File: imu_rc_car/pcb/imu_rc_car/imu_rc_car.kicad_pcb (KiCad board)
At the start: 2 copper layers, 100.8 x 82.3 mm, 0 parts

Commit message: commit #26
started work car pcb
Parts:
- added C10: 10uF, Capacitor_SMD:C_1206_3216Metric_Pad1.33x1.80mm_HandSolder, F.Cu at (168.7, 98.1)
- added C11: 0.1uF, Capacitor_SMD:C_1206_3216Metric_Pad1.33x1.80mm_HandSolder, F.Cu at (167.1, 116.6)
- added C12: 10uF, Capacitor_SMD:C_1206_3216Metric_Pad1.33x1.80mm_HandSolder, F.Cu at (167.1, 121.1)
- added C13: 0.1uF, Capacitor_SMD:C_1206_3216Metric_Pad1.33x1.80mm_HandSolder, F.Cu at (180.9, 109.6)
- added C14: 10uF, Capacitor_SMD:C_1206_3216Metric_Pad1.33x1.80mm_HandSolder, F.Cu at (183.5, 109.6)
- added C15: 0.1uF, Capacitor_SMD:C_1206_3216Metric_Pad1.33x1.80mm_HandSolder, F.Cu at (178.3, 109.6)
- added C16: 10uF, Capacitor_SMD:C_1206_3216Metric_Pad1.33x1.80mm_HandSolder, F.Cu at (175.6, 109.6)
- added C7: 1uF/16V, Capacitor_SMD:C_0805_2012Metric, F.Cu at (164.4, 73.4)
- added C8: 1uF/16V, Capacitor_SMD:C_0805_2012Metric, F.Cu at (164.4, 76.9)
- added C9: 0.1uF, Capacitor_SMD:C_1206_3216Metric_Pad1.33x1.80mm_HandSolder, F.Cu at (168.7, 102.1)
- added J1: Encoder FS, Connector_JST:JST_PH_S4B-PH-K_1x04_P2.00mm_Horizontal, F.Cu at (146.0, 62.0)
- added J10: Prox Sensor RS, Connector_JST:JST_PH_S5B-PH-K_1x05_P2.00mm_Horizontal, F.Cu at (136.0, 128.6)
- added J11: Prox Sensor LS, Connector_JST:JST_PH_S5B-PH-K_1x05_P2.00mm_Horizontal, F.Cu at (121.0, 128.6)
- added J12: Prox Sensor BS, Connector_JST:JST_PH_S5B-PH-K_1x05_P2.00mm_Horizontal, F.Cu at (106.0, 128.6)
- added J2: Encoder BS, Connector_JST:JST_PH_S4B-PH-K_1x04_P2.00mm_Horizontal, F.Cu at (165.5, 62.0)
- added J7: Left Terminal, TerminalBlock:TerminalBlock_Xinya_XY308-2.54-4P_1x04_P2.54mm_Horizontal, F.Cu at (165.4, 131.5)
- added J8: Right Terminal, TerminalBlock:TerminalBlock_Xinya_XY308-2.54-4P_1x04_P2.54mm_Horizontal, F.Cu at (177.4, 131.5)
- added J9: Prox Sensor FS, Connector_JST:JST_PH_S5B-PH-K_1x05_P2.00mm_Horizontal, F.Cu at (151.0, 128.6)
- added Q5: IRLML6344TRPBF, Package_TO_SOT_SMD:SOT-23, F.Cu at (146.4, 74.8)
- added Q6: DMP3160L-7, Package_TO_SOT_SMD:SOT-23, F.Cu at (140.5, 74.9)
- added R10: 6k, Resistor_SMD:R_0805_2012Metric, F.Cu at (142.5, 79.9)
- added R8: 10k, Resistor_SMD:R_0805_2012Metric, F.Cu at (144.9, 70.9)
- added R9: 22k, Resistor_SMD:R_0805_2012Metric, F.Cu at (147.3, 79.9)
- added U1: ESP32-S3-DevKitC, PCM_Espressif:ESP32-S3-DevKitC, F.Cu at (127.9, 117.3)
- added U2: TB6612FNG, Package_SO:SSOP-24_5.3x8.2mm_P0.65mm, F.Cu at (168.7, 109.1)
- added U3: AP2112K-3.3, Package_TO_SOT_SMD:SOT-23-5, F.Cu at (159.9, 74.7)
- added U4: TB6612FNG, Package_SO:SSOP-24_5.3x8.2mm_P0.65mm, F.Cu at (181.9, 117.3)
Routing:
- net +3V3: track 0.00 -> 78.5 mm
- net Net-(Q5-D): track 0.00 -> 20.5 mm
- net +BATT: track 0.00 -> 13.6 mm
- net Net-(Q6-S): track 0.00 -> 4.13 mm
- net BATT_READ: track 0.00 -> 3.00 mm
- added copper zone on F.Cu, net GND
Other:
- board size 100.8 x 82.3 mm -> 100 x 82.3 mm

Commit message: commit #27
revision for hand unit complete (board is ready)
board for proximity sensors in series
minor revision in encoder board
progressing work in car board
added essential libraries support for 3D components
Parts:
- removed C7, C8: 1uF/16V, Capacitor_SMD:C_0805_2012Metric
- removed J10: Prox Sensor RS, Connector_JST:JST_PH_S5B-PH-K_1x05_P2.00mm_Horizontal
- removed J11: Prox Sensor LS, Connector_JST:JST_PH_S5B-PH-K_1x05_P2.00mm_Horizontal
- removed J12: Prox Sensor BS, Connector_JST:JST_PH_S5B-PH-K_1x05_P2.00mm_Horizontal
- removed Q5: IRLML6344TRPBF, Package_TO_SOT_SMD:SOT-23
- removed Q6: DMP3160L-7, Package_TO_SOT_SMD:SOT-23
- removed U4: TB6612FNG, Package_SO:SSOP-24_5.3x8.2mm_P0.65mm
- added C1: 10uF, Capacitor_SMD:CP_Elec_5x5.7, F.Cu at (184.1, 68.4)
- added J3: Encoder B, IMURCLibrary:JST_PH_S4B-PH-SM4-TB_1x04-1MP_P2.00mm_Horizontal, B.Cu at (145.0, 131.8)
- added J4: Prox Sensor FS, IMURCLibrary:JST_PH_S5B-PH-SM4-TB_1x05-1MP_P2.00mm_Horizontal, F.Cu at (127.3, 131.8)
- added J5: Prox Sensor LS, IMURCLibrary:JST_PH_S5B-PH-SM4-TB_1x05-1MP_P2.00mm_Horizontal, B.Cu at (127.3, 131.8)
- added J6: Prox Sensor RS, IMURCLibrary:JST_PH_S5B-PH-SM4-TB_1x05-1MP_P2.00mm_Horizontal, B.Cu at (162.7, 131.8)
- added JP1: SolderJumper_2_Open, Jumper:SolderJumper-2_P1.3mm_Open_RoundedPad1.0x1.5mm, F.Cu at (145.0, 121.1)
- added Q1: DMP3160L-7, Package_TO_SOT_SMD:SOT-23, F.Cu at (180.9, 93.9)
- added Q2: IRLML6344TRPBF, Package_TO_SOT_SMD:SOT-23, F.Cu at (180.9, 98.5)
- added SW1: SW_Nidec_CAS-120A1, Button_Switch_SMD:Nidec_Copal_CAS-120A, F.Cu at (166.7, 74.7)
- J1: value Encoder FS -> LiPo Battery; footprint Connector_JST:JST_PH_S4B-PH-K_1x04_P2.00mm_Horizontal -> IMURCLibrary:AMASS_XT60IPW-M_1x03_P7.20mm_Horizontal; moved to B.Cu
- J2: value Encoder BS -> Encoder F; footprint Connector_JST:JST_PH_S4B-PH-K_1x04_P2.00mm_Horizontal -> IMURCLibrary:JST_PH_S4B-PH-SM4-TB_1x04-1MP_P2.00mm_Horizontal
- J7: value Left Terminal -> Prox Sensor BS; footprint TerminalBlock:TerminalBlock_Xinya_XY308-2.54-4P_1x04_P2.54mm_Horizontal -> IMURCLibrary:JST_PH_S5B-PH-SM4-TB_1x05-1MP_P2.00mm_Horizontal
- J8: value Right Terminal -> Left Terminal; footprint TerminalBlock:TerminalBlock_Xinya_XY308-2.54-4P_1x04_P2.54mm_Horizontal -> IMURCLibrary:TerminalBlock_Xinya_XY308-2.54-4P_1x04_P2.54mm_Horizontal
- J9: value Prox Sensor FS -> Right Terminal; footprint Connector_JST:JST_PH_S5B-PH-K_1x05_P2.00mm_Horizontal -> IMURCLibrary:TerminalBlock_Xinya_XY308-2.54-4P_1x04_P2.54mm_Horizontal
- R10: value 6k -> 51k
- R9: value 22k -> 33k
- U1: footprint PCM_Espressif:ESP32-S3-DevKitC -> IMURCLibrary:ESP32-S3-DevKitC
- U3: value AP2112K-3.3 -> TB6612FNG; footprint Package_TO_SOT_SMD:SOT-23-5 -> Package_SO:SSOP-24_5.3x8.2mm_P0.65mm
- moved J2 72.7 mm to (145.0, 131.8), turned to 0 degrees
- moved J8 71.3 mm to (106.1, 131.6)
- moved C9 65.2 mm to (104.3, 112.0), turned to 90 degrees
- moved C10 62.6 mm to (107.7, 112.0), turned to 90 degrees
- moved U2 59.8 mm to (109.9, 119.8)
- moved C11 56.3 mm to (111.0, 112.0), turned to 90 degrees
- moved C12 53.5 mm to (114.3, 112.0), turned to 90 degrees
- moved U3 49.4 mm to (180.1, 119.8), turned to 90 degrees
- moved R10 38.5 mm to (175.7, 99.2)
- moved R8 38.1 mm to (175.7, 93.3), turned to 0 degrees
- moved R9 32.8 mm to (175.7, 96.3)
- moved J1 30.1 mm to (175.3, 68.8)
- moved U1 29.5 mm to (156.4, 110.1)
- moved J9 25.5 mm to (176.3, 131.6)
- moved C16 10.1 mm to (185.5, 112.1)
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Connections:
- C10 pad 2: MOTOR4- -> GND
- C11 pad 1: 7.4V -> +7V4
- C11 pad 2: MOTOR4- -> GND
- C12 pad 1: 7.4V -> +7V4
- C12 pad 2: MOTOR4- -> GND
- C13 pad 2: MOTOR4- -> GND
- C14 pad 2: MOTOR4- -> GND
- C15 pad 1: 7.4V -> +7V4
- C15 pad 2: MOTOR4- -> GND
- C16 pad 1: 7.4V -> +7V4
- C16 pad 2: MOTOR4- -> GND
- C9 pad 2: MOTOR4- -> GND
- J1 pad 1: ENC2 -> GND
- J1 pad 2: ENC1 -> Net-(J1-Pin_2)
- J1 pad 3: MOTOR4- -> (no net)
- J2 pad 1: ENC4 -> ENC2
- J2 pad 2: ENC3 -> ENC1
- J2 pad 3: MOTOR4- -> GND
- J7 pad 1: MOTOR2- -> PRX_BS
- J7 pad 2: MOTOR2+ -> GND
- J7 pad 3: MOTOR1- -> +3V3
- J7 pad 4: MOTOR1+ -> Net-(J6-Pin_5)
- J8 pad 1: MOTOR4- -> MOTOR_FL+
- J8 pad 2: MOTOR4+ -> MOTOR_FL-
- J8 pad 3: MOTOR3- -> MOTOR_RL-
- J8 pad 4: MOTOR3+ -> MOTOR_RL+
- J9 pad 1: PRX_FS -> MOTOR_RR+
- J9 pad 2: MOTOR4- -> MOTOR_RR-
- J9 pad 3: +3V3 -> MOTOR_FR-
- J9 pad 4: SI -> MOTOR_FR+
- R8 pad 2: +BATT -> +7V4
- R9 pad 2: MOTOR4- -> GND
- U1 pad 22: MOTOR4- -> GND
- U1 pad 23: MOTOR4- -> GND
- U1 pad 24: MOTOR4- -> GND
- U1 pad 44: MOTOR4- -> GND
- U2 pad 1: MOTOR1+ -> MOTOR_FL+
- U2 pad 11: MOTOR2+ -> MOTOR_RL+
- U2 pad 12: MOTOR2+ -> MOTOR_RL+
- U2 pad 13: 7.4V -> +7V4
- U2 pad 14: 7.4V -> +7V4
- U2 pad 2: MOTOR1+ -> MOTOR_FL+
- U2 pad 24: 7.4V -> +7V4
- U2 pad 5: MOTOR1- -> MOTOR_FL-
- U2 pad 6: MOTOR1- -> MOTOR_FL-
- U2 pad 7: MOTOR2- -> MOTOR_RL-
- U2 pad 8: MOTOR2- -> MOTOR_RL-
- U3 pad 1: +BATT -> MOTOR_RR+
- U3 pad 2: GND -> MOTOR_RR+
- U3 pad 3: +BATT -> GND
- U3 pad 4: unconnected-(U3-NC-Pad4) -> GND
- U3 pad 5: +3V3 -> MOTOR_RR-
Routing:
- net +3V3: track 78.5 -> 0.00 mm
- net Net-(Q1-G): track 20.5 -> 0.00 mm
- net +BATT: track 13.6 -> 0.00 mm
- net Net-(Q1-S): track 4.13 -> 0.00 mm
- net BATT_READ: track 3.00 -> 0.00 mm
- added copper zone on B.Cu, net GND

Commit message: commit #28
added 3d file for esp32s3
progression with car pcb
minor changes prox sensors test board
final revision hand unit
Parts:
- removed C16: 10uF, Capacitor_SMD:C_1206_3216Metric_Pad1.33x1.80mm_HandSolder
- removed U2: TB6612FNG, Package_SO:SSOP-24_5.3x8.2mm_P0.65mm
- added C8: 10uF, Capacitor_SMD:C_0805_2012Metric, F.Cu at (119.2, 94.0)
- added Q1: IRLZ34N, Package_TO_SOT_SMD:TO-263-2_TabPin1, F.Cu at (103.7, 73.2)
- added R11: 22, Resistor_SMD:R_0805_2012Metric, F.Cu at (111.1, 76.5)
- added R12: 100k, Resistor_SMD:R_0805_2012Metric, F.Cu at (111.1, 72.7)
- added U6: DRV8833PWP, Package_SO:HTSSOP-16-1EP_4.4x5mm_P0.65mm_EP3.4x5mm_Mask2.46x2.31mm_ThermalVias, B.Cu at (180.1, 122.3)
- added U7: DRV8833PWP, Package_SO:HTSSOP-16-1EP_4.4x5mm_P0.65mm_EP3.4x5mm_Mask2.46x2.31mm_ThermalVias, B.Cu at (109.9, 122.3)
- C10, C12: value 10uF -> 2.2uF; footprint Capacitor_SMD:C_1206_3216Metric_Pad1.33x1.80mm_HandSolder -> Capacitor_SMD:C_0805_2012Metric; moved to B.Cu
- C11, C9: value 0.1uF -> 10nF; footprint Capacitor_SMD:C_1206_3216Metric_Pad1.33x1.80mm_HandSolder -> Capacitor_SMD:C_0805_2012Metric; moved to B.Cu
- C13, C15: value 0.1uF -> 100nF; footprint Capacitor_SMD:C_1206_3216Metric_Pad1.33x1.80mm_HandSolder -> Capacitor_SMD:C_0805_2012Metric
- C14: footprint Capacitor_SMD:C_1206_3216Metric_Pad1.33x1.80mm_HandSolder -> Capacitor_SMD:C_0805_2012Metric
- J3: renamed from J1; footprint IMURCLibrary:AMASS_XT60IPW-M_1x03_P7.20mm_Horizontal -> TerminalBlock:TerminalBlock_MaiXu_MX126-5.0-02P_1x02_P5.00mm
- JP1: moved to B.Cu
- SW1: footprint Button_Switch_SMD:Nidec_Copal_CAS-120A -> Button_Switch_THT:SW_Slide_SPDT_Angled_CK_OS102011MA1Q
- U1: footprint IMURCLibrary:ESP32-S3-DevKitC -> PCM_Espressif:ESP32-S3-DevKitC
- U3: value TB6612FNG -> AMS1117-3.3; footprint Package_SO:SSOP-24_5.3x8.2mm_P0.65mm -> Package_TO_SOT_SMD:SOT-223-3_TabPin2
- moved C1 85.0 mm to (105.0, 99.8), turned to 90 degrees
- moved J3 76.0 mm to (110.5, 108.4)
- moved SW1 75.1 mm to (97.4, 103.7)
- moved C9 74.4 mm to (178.6, 115.5)
- moved C10 73.5 mm to (181.1, 115.5)
- moved Q5 70.0 mm to (111.3, 91.1), turned to -90 degrees
- moved Q6 69.6 mm to (111.3, 95.4), turned to -90 degrees
- moved R10 65.8 mm to (111.4, 85.5)
- moved R9 64.9 mm to (111.4, 87.8), turned to 180 degrees
- moved R8 63.8 mm to (112.2, 98.7), turned to 180 degrees
- moved C14 63.7 mm to (119.2, 99.2), turned to 180 degrees
- moved U3 58.8 mm to (126.2, 96.5), turned to 0 degrees
- moved C15 56.4 mm to (119.2, 96.6), turned to 180 degrees
- moved C13 55.6 mm to (122.8, 102.4), turned to -90 degrees
- moved C12 4.96 mm to (110.9, 115.5)
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- renumbered J2 to J1, J5 to J10, J6 to J11, J7 to J12, J3 to J2, J8 to J7, J9 to J8, J4 to J9, Q2 to Q5, Q1 to Q6
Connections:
- C10 pad 1: +3V3 -> +7V4
- C11 pad 1: +7V4 -> Net-(U7-VCP)
- C13 pad 1: +3V3 -> +7V4
- C14 pad 1: +3V3 -> +7V4
- C15 pad 1: +7V4 -> +3V3
- C9 pad 1: +3V3 -> Net-(U6-VCP)
- J7 pad 3: MOTOR_RL- -> MOTOR_RL+
- J7 pad 4: MOTOR_RL+ -> MOTOR_RL-
- J8 pad 3: MOTOR_FR- -> MOTOR_FR+
- J8 pad 4: MOTOR_FR+ -> MOTOR_FR-
- U1 pad 11: BIN1 -> unconnected-(U1-GPIO18/ADC2_CH7-Pad11)
- U1 pad 12: PWMC -> unconnected-(U1-GPIO8/ADC1_CH7-Pad12)
- U1 pad 15: PWMD -> unconnected-(U1-GPIO9/ADC1_CH8-Pad15)
- U1 pad 16: STBYA -> unconnected-(U1-GPIO10/ADC1_CH9-Pad16)
- U1 pad 17: AIN3 -> unconnected-(U1-GPIO11/ADC2_CH0-Pad17)
- U1 pad 18: AIN4 -> unconnected-(U1-GPIO12/ADC2_CH1-Pad18)
- U1 pad 25: BIN2 -> unconnected-(U1-GPIO19/USB_D--Pad25)
- U1 pad 26: BIN3 -> BATT_READ
- U1 pad 27: BIN4 -> BATT_READ_EN
- U1 pad 28: unconnected-(U1-GPIO47-Pad28) -> BIN1
- U1 pad 29: unconnected-(U1-GPIO48-Pad29) -> BIN2
- U1 pad 30: unconnected-(U1-GPIO45-Pad30) -> AIN2
- U1 pad 32: BATT_READ -> AIN1
- U1 pad 33: BATT_READ_EN -> STBYA
- U1 pad 34: unconnected-(U1-GPIO37-Pad34) -> PRX_FS
- U1 pad 35: unconnected-(U1-GPIO38-Pad35) -> PRX_LS
- U1 pad 36: unconnected-(U1-GPIO39/MTCK-Pad36) -> ENC4
- U1 pad 37: unconnected-(U1-GPIO40/MTDO-Pad37) -> ENC3
- U1 pad 38: unconnected-(U1-GPIO41/MTDI-Pad38) -> ENC1
- U1 pad 39: unconnected-(U1-GPIO42/MTMS-Pad39) -> ENC2
- U1 pad 4: AIN1 -> PRX_RS
- U1 pad 5: AIN2 -> PRX_BS
- U1 pad 6: PWMA -> BIN3
- U1 pad 7: PWMB -> BIN4
- U1 pad 8: unconnected-(U1-GPIO15/ADC2_CH4/32K_P-Pad8) -> AIN4
- U1 pad 9: unconnected-(U1-GPIO16/ADC2_CH5/32K_N-Pad9) -> AIN3
- U3 pad 1: MOTOR_RR+ -> GND
- U3 pad 2: MOTOR_RR+ -> +3V3
- U3 pad 3: GND -> +7V4
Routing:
- net SO: track 0.00 -> 129.8 mm, vias 0 -> 2
- net +7V4: track 0.00 -> 122.5 mm, vias 0 -> 4
- net BIN1: track 0.00 -> 65.5 mm
- net BIN2: track 0.00 -> 63.7 mm
- net STBYA: track 0.00 -> 56.1 mm
- net AIN2: track 0.00 -> 54.7 mm
- net STBYB: track 0.00 -> 54.0 mm
- net AIN1: track 0.00 -> 51.9 mm
- net PRX_BS: track 0.00 -> 49.4 mm, vias 0 -> 1
- net PRX_FS: track 0.00 -> 49.3 mm, vias 0 -> 1
- net ENC4: track 0.00 -> 47.5 mm
- net ENC3: track 0.00 -> 44.4 mm
- net PRX_LS: track 0.00 -> 43.3 mm
- net AIN3: track 0.00 -> 43.1 mm
- net Net-(J10-Pin_5): track 0.00 -> 41.8 mm
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- added copper zone on F.Cu, net +3V3
- added copper zone on F.Cu, net +7V4

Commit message: commit #29
fixed board issue with PWM circuit driver
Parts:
- R11: value 22 -> 10
- moved Q1 74.3 mm to (176.6, 87.2), turned to 0 degrees
- moved R11 54.1 mm to (163.3, 90.7), turned to -90 degrees
- moved R12 53.7 mm to (163.3, 85.6)
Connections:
- Q1 pad 1: +7V4 -> PWM
- Q1 pad 2: SO -> Net-(Q1-D)
- R11 pad 1: Net-(Q1-S) -> Net-(Q1-D)
- R11 pad 2: GND -> SO
- R12 pad 1: +7V4 -> PWM
- U1 pad 11: unconnected-(U1-GPIO18/ADC2_CH7-Pad11) -> PWM
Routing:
- net SO: track 129.8 -> 38.7 mm, vias 2 -> 0
- net PWM: track 0.00 -> 22.8 mm
- net +7V4: track 122.5 -> 134.9 mm, vias 4 -> 2
- net Net-(Q1-D): track 0.00 -> 5.71 mm
- net Net-(J10-Pin_5): track 41.8 -> 44.7 mm
- net Net-(J11-Pin_5): track 28.2 -> 30.9 mm
- net PRX_BS: track 49.4 -> 51.9 mm
- net Net-(Q6-S): track 12.2 -> 14.1 mm
- net Net-(J10-Pin_4): track 27.2 -> 29.0 mm
- net PRX_LS: track 43.3 -> 44.9 mm
- net BATT_READ_EN: track 35.7 -> 34.1 mm
- net ENC3: track 44.4 -> 44.9 mm
- net GND: vias 1030 -> 1019
- net +3V3: vias 0 -> 70
- added copper zone on B.Cu, net +3V3

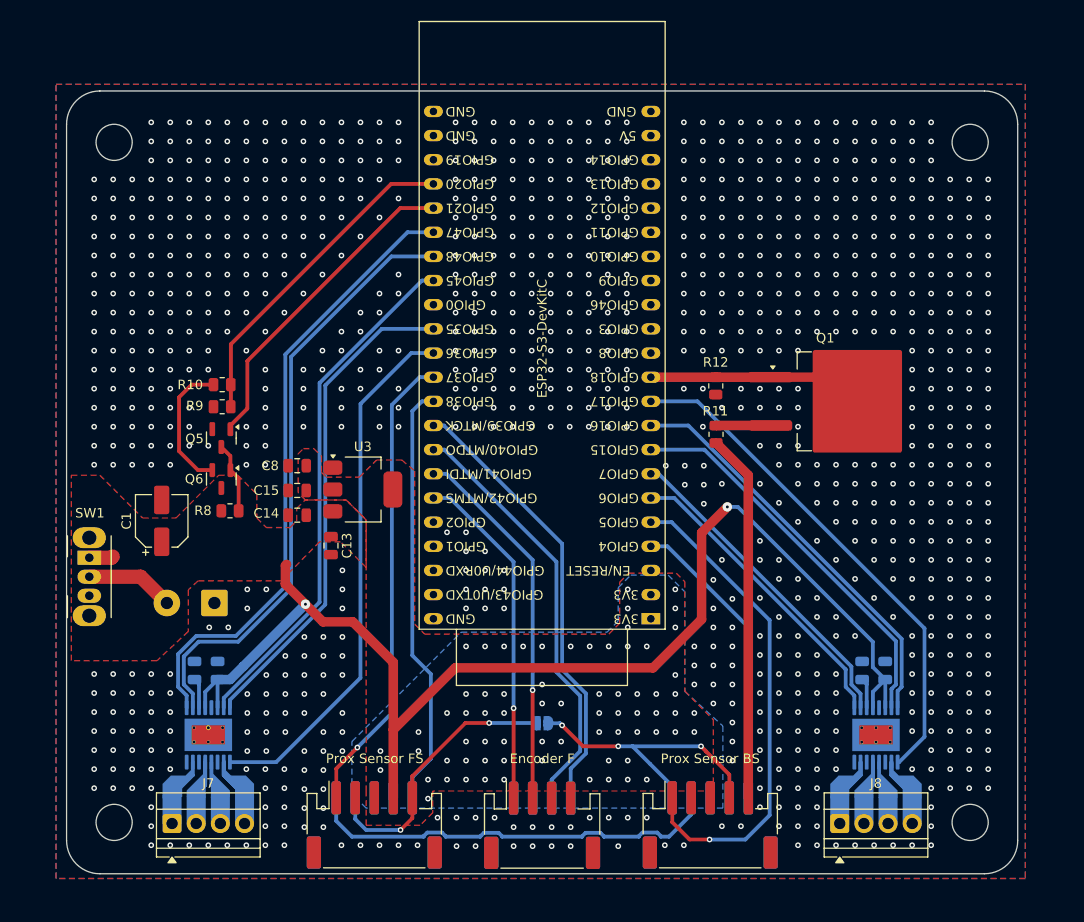
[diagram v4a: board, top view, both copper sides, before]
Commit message: commit #30
changed 3d model offset in esp32s3
imported mouse-bites to kicad
final changes in imu-rc car before revision
critical change in pins 3 and 4 of optical sensor which were switched (encoder board)
removed test unit
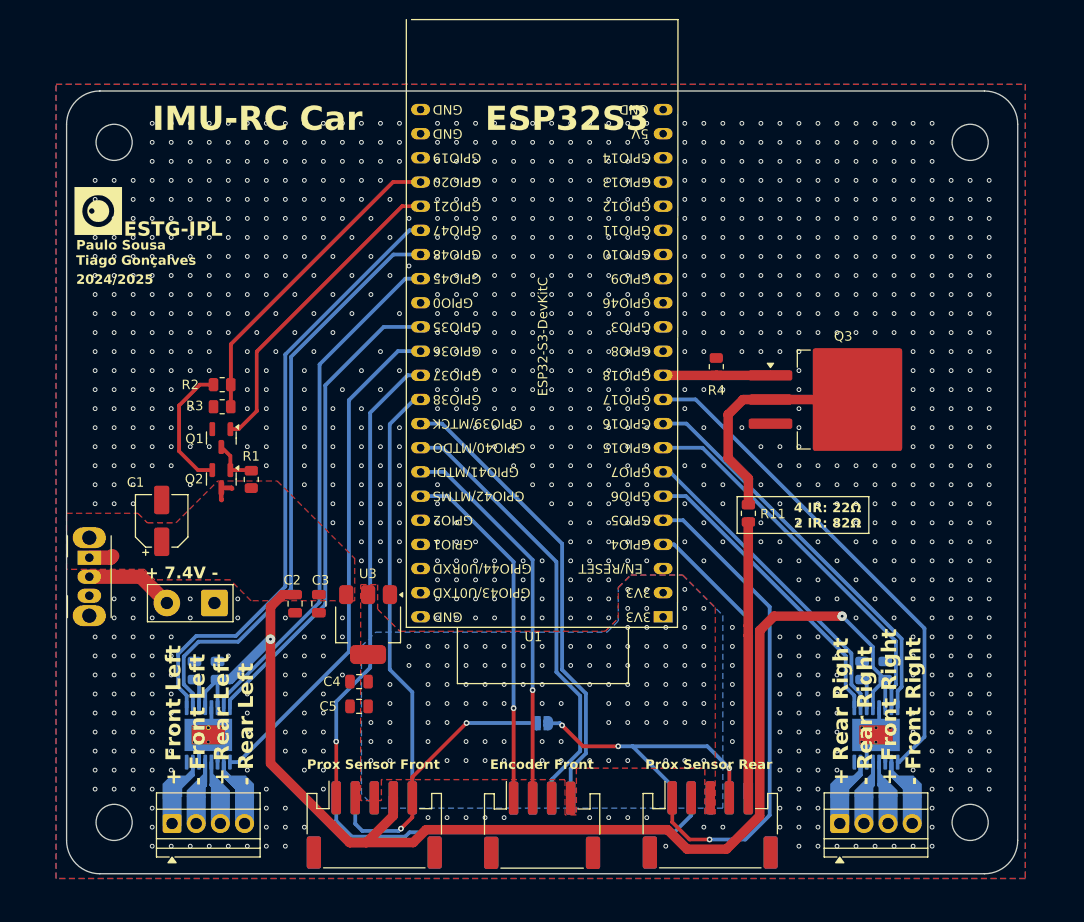
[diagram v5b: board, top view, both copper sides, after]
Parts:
- removed the J7 at (106.1, 131.6)
- added G***: LOGO, LOGO, F.Cu at (98.3, 67.2)
- added J2: Left Terminal, IMURCLibrary:TerminalBlock_Xinya_XY308-2.54-4P_1x04_P2.54mm_Horizontal, F.Cu at (106.1, 131.6)
- Q3: renamed from Q1; footprint Package_TO_SOT_SMD:TO-263-2_TabPin1 -> Package_TO_SOT_SMD:TO-263-3_TabPin2
- U1: footprint PCM_Espressif:ESP32-S3-DevKitC -> IMURCLibrary:ESP32-S3-DevKitC
- moved C4 23.6 mm to (125.8, 116.7)
- moved C5 23.6 mm to (125.8, 119.3)
- moved U3 14.2 mm to (126.7, 110.7), turned to -90 degrees
- moved C2 9.31 mm to (119.0, 108.5), turned to -90 degrees
- moved R11 8.98 mm to (166.7, 99.0)
- moved C3 6.24 mm to (121.5, 108.5)
- moved R1 3.99 mm to (114.4, 95.4), turned to -90 degrees
- moved R4 2.02 mm to (163.3, 83.6), turned to 90 degrees
- moved U1 1.36 mm to (155.1, 109.9)
- moved Q3 0.19 mm to (176.7, 87.0)
- renumbered C14 to C2, C13 to C3, C8 to C4, C15 to C5, C12 to C6, C11 to C7, C10 to C8, J3 to J1, J8 to J3, J9 to J4, J10 to J5, J11 to J6, J12 to J7, J1 to J8, J2 to J9, Q5 to Q1, Q6 to Q2, R8 to R1, R10 to R2, R9 to R3, R12 to R4
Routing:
- net GND: track 0.00 -> 19.1 mm, vias 1019 -> 1120
- net Net-(Q3-D): track 5.71 -> 24.6 mm
- net +7V4: track 134.9 -> 147.4 mm
- net PWM: track 22.8 -> 11.3 mm
- net SO: track 38.7 -> 29.0 mm
- net STBYA: track 56.1 -> 53.4 mm
- net Net-(Q1-D): track 7.47 -> 5.05 mm
- net Net-(J5-Pin_5): track 44.7 -> 43.2 mm
- net ENC4: track 47.1 -> 48.6 mm
- net ENC2: track 36.1 -> 37.5 mm
- net ENC1: track 39.2 -> 40.7 mm
- net ENC3: track 44.9 -> 46.4 mm
- net BIN1: track 65.5 -> 64.3 mm
- net BIN2: track 63.7 -> 62.5 mm
- net BATT_READ: track 34.9 -> 33.6 mm
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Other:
- board text added: "+ 7.4V -"
- board text added: "+ Front Left - Front Left + Rear Left - Rear Left"
- board text added: "+ Rear Right - Rear Right + Front Right - Front Right"
- board text added: "2 Prox Sensors"
- board text added: "2024/2025"
- board text added: "4 IR: 22Ω 2 IR: 82Ω"
- board text added: "ESP32S3"
- board text added: "ESTG-IPL"
- board text added: "Encoder Front"
- board text added: "Encoder Rear"
- board text added: "IMU-RC Car"
- board text added: "Paulo Sousa Tiago Gonçalves"
- board text added: "Prox Sensor Front"
- board text added: "Prox Sensor Left"
- board text added: "Prox Sensor Rear"
- board text added: "Prox Sensor Right"
- board text added: "v1.0.0"
